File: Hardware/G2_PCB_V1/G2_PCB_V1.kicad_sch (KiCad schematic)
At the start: 21 parts, among them P1 Ultrasonido, P2 Ultrasonido, P3 Ultrasonido, P4 EncoderDerecho, P5 EncoderIzquierdo, P6 Bateria, P7 Driver L9110, SW1 SW_Push, SW2 SW_Push, SW3 SW_Push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

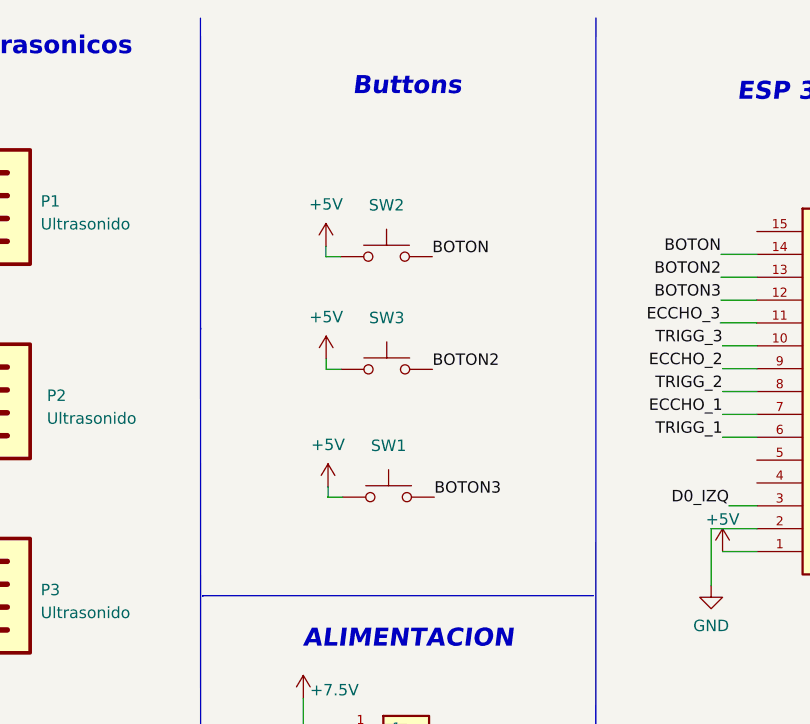
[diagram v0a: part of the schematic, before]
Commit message: comence a desarrollar un modulo para la mpu9150, PCB terminado listo para fabricar y probar su funcionamiento
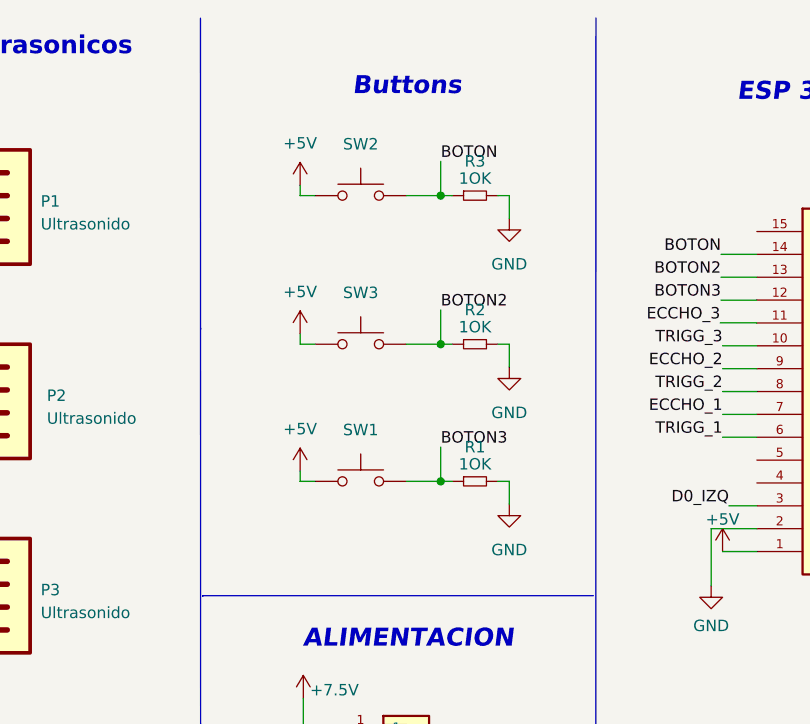
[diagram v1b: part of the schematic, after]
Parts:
- added R1, R2, R3: 1OK, EESTN5:R_1206, symbol EESTN5:R
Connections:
- net BOTON: now also R3.1
- net BOTON2: now also R2.1
- net BOTON3: now also R1.1
- net GND: now also R1.2, R2.2, R3.2
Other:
- moved on the sheet: SW1, SW2, SW3
